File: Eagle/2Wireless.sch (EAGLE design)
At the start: 19 parts, among them IC1 TCA9517A, IC3 MB85RS2MTAPNF-G-BDERE1

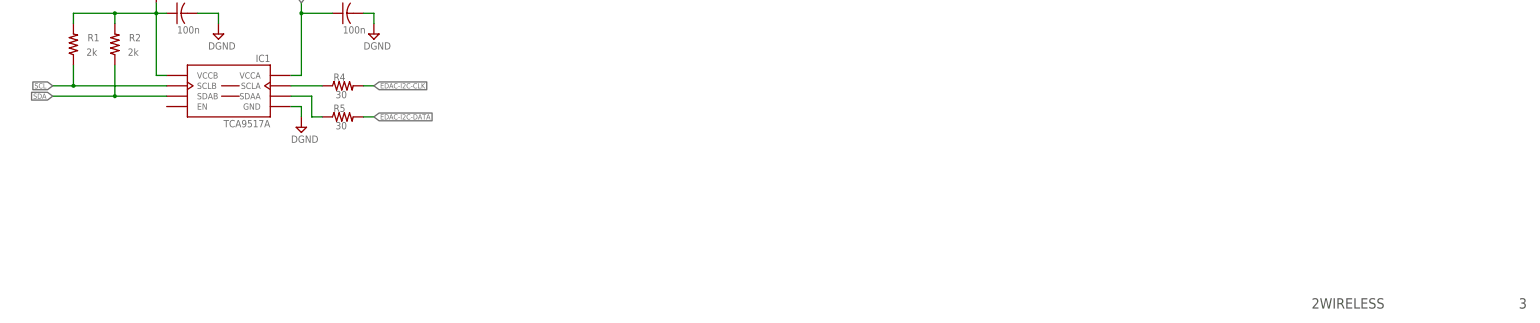
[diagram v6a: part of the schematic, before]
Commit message: Add blue LED for I2C activity
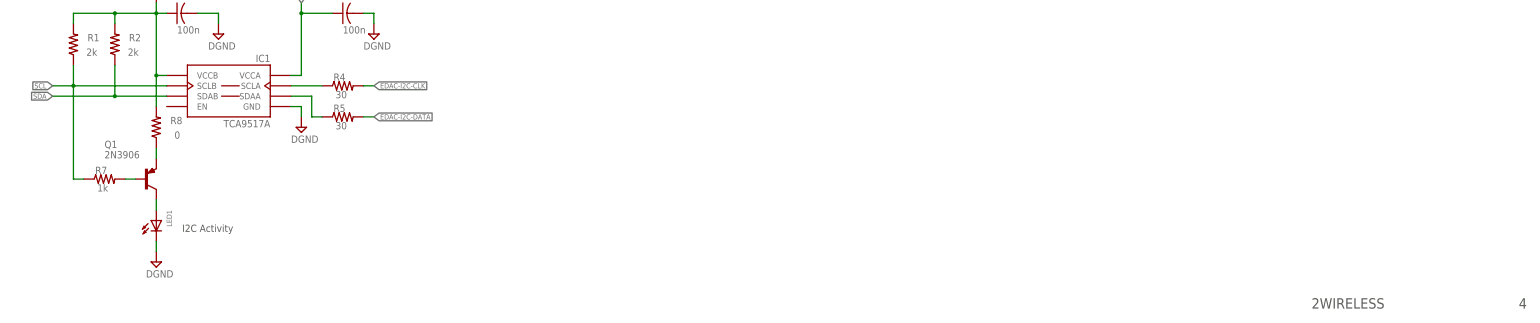
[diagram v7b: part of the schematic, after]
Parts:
- added LED1: (no value), studio_h:LED0805BLUE
- added Q1: 2N3906, studio_h:PNPMMBT3906
- added R7: 1k, studio_h:RB
- added R8: 0, studio_h:RB
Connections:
- new net N$1: Q1.B, R7.2
- new net N$2: LED1.A, Q1.C
- new net N$3: Q1.E, R8.1
- net DGND: now also LED1.C
- net DPWR: now also R8.2
- net SCL: now also R7.1
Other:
- note added: "4"
- note added: "I2C Activity"
- note removed: "3"
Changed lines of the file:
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@@
 <setting verticaltext="up"/>
 </settings>
-<grid distance="0.1" unitdist="inch" unit="inch" style="lines" multiple="1" display="no" altdistance="0.01" altunitdist="inch" altunit="inch"/>
+<grid distance="0.1" unitdist="inch" unit="inch" style="lines" multiple="1" display="yes" altdistance="0.01" altunitdist="inch" altunit="inch"/>
 <layers>
 <layer number="1" name="Top" color="4" fill="1" visible="no" active="no"/>
@@
 <part name="R1" library="studio_h" deviceset="R" device="B" value="2k"/>
 <part name="R2" library="studio_h" deviceset="R" device="B" value="2k"/>
+<part name="Q1" library="studio_h" deviceset="PNP" device="MMBT3906" value="2N3906"/>
+<part name="R7" library="studio_h" deviceset="R" device="B" value="1k"/>
+<part name="R8" library="studio_h" deviceset="R" device="B" value="0"/>
+<part name="LED1" library="studio_h" deviceset="LED" device="0805BLUE"/>
+<part name="DGND2" library="studio_h" deviceset="DGND" device=""/>
 </parts>
 <sheets>
@@
 <plain>
 <text x="367.03" y="6.35" size="2.54" layer="97" font="vector" ratio="12">2WIRELESS</text>
-<text x="417.83" y="6.35" size="2.54" layer="97" font="vector" ratio="12">3</text>
+<text x="417.83" y="6.35" size="2.54" layer="97" font="vector" ratio="12">4</text>
 <text x="229.616" y="160.02" size="6.4516" layer="97" font="vector" ratio="12">5V Power</text>
 <text x="237.236" y="233.172" size="6.4516" layer="97" font="vector" ratio="12">Memory</text>
@@
 <text x="40.64" y="137.16" size="2.54" layer="97" font="vector" ratio="12">V2</text>
 <text x="53.34" y="149.86" size="2.54" layer="97" font="vector" ratio="12">AUX</text>
+<text x="90.17" y="25.146" size="1.778" layer="97" font="vector" ratio="12">I2C Activity</text>
 </plain>
 <instances>
@@
 <attribute name="VALUE" x="79.502" y="70.104" size="1.778" layer="96" font="vector" ratio="12" rot="R180"/>
 </instance>
+<instance part="Q1" gate="G$1" x="81.28" y="38.1"/>
+<instance part="R7" gate="G$1" x="71.12" y="38.1" smashed="yes">
+<attribute name="NAME" x="68.834" y="39.3446" size="1.778" layer="95" font="vector" ratio="12"/>
+<attribute name="VALUE" x="69.342" y="35.052" size="1.778" layer="96" font="vector" ratio="12"/>
+</instance>
+<instance part="R8" gate="G$1" x="83.82" y="50.8" smashed="yes" rot="R90">
+<attribute name="NAME" x="90.1954" y="53.34" size="1.778" layer="95" font="vector" ratio="12" rot="R180"/>
+<attribute name="VALUE" x="89.662" y="49.784" size="1.778" layer="96" font="vector" ratio="12" rot="R180"/>
+</instance>
+<instance part="LED1" gate="G$1" x="83.82" y="25.4" rot="R270"/>
+<instance part="DGND2" gate="G$1" x="83.82" y="17.78"/>
 </instances>
 <busses>
@@
 <wire x1="63.5" y1="66.04" x2="63.5" y2="60.96" width="0.1524" layer="91"/>
 <junction x="63.5" y="60.96"/>
+<pinref part="R7" gate="G$1" pin="1"/>
+<wire x1="66.04" y1="38.1" x2="63.5" y2="38.1" width="0.1524" layer="91"/>
+<wire x1="63.5" y1="38.1" x2="63.5" y2="60.96" width="0.1524" layer="91"/>
 </segment>
 <segment>
@@
 <wire x1="129.54" y1="180.34" x2="129.54" y2="177.8" width="0.1524" layer="91"/>
 <pinref part="J5" gate="G$1" pin="11"/>
+</segment>
+<segment>
+<pinref part="LED1" gate="G$1" pin="C"/>
+<pinref part="DGND2" gate="G$1" pin="DGND"/>
+<wire x1="83.82" y1="20.32" x2="83.82" y2="22.86" width="0.1524" layer="91"/>
 </segment>
 </net>
@@
 <wire x1="73.66" y1="78.74" x2="83.82" y2="78.74" width="0.1524" layer="91"/>
 <junction x="73.66" y="78.74"/>
+<pinref part="R8" gate="G$1" pin="2"/>
+<wire x1="83.82" y1="55.88" x2="83.82" y2="63.5" width="0.1524" layer="91"/>
+<junction x="83.82" y="63.5"/>
 </segment>
 <segment>
@@
 </segment>
 </net>
+<net name="N$1" class="0">
+<segment>
+<pinref part="Q1" gate="G$1" pin="B"/>
+<pinref part="R7" gate="G$1" pin="2"/>
+<wire x1="76.2" y1="38.1" x2="78.74" y2="38.1" width="0.1524" layer="91"/>
+</segment>
+</net>
+<net name="N$2" class="0">
+<segment>
+<pinref part="Q1" gate="G$1" pin="C"/>
+<pinref part="LED1" gate="G$1" pin="A"/>
+<wire x1="83.82" y1="30.48" x2="83.82" y2="33.02" width="0.1524" layer="91"/>
+</segment>
+</net>
+<net name="N$3" class="0">
+<segment>
+<pinref part="R8" gate="G$1" pin="1"/>
+<pinref part="Q1" gate="G$1" pin="E"/>
+<wire x1="83.82" y1="45.72" x2="83.82" y2="43.18" width="0.1524" layer="91"/>
+</segment>
+</net>
